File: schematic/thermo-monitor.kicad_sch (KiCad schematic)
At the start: 17 parts, among them J1 AudioJack4, J2 AudioJack4, J3 AudioJack4, J4 AudioJack4, J5 AudioJack4, J6 Barrel_Jack_Switch, SW1 SW_Push_Dual_x2, SW2 SW_Push_Dual_x2, U3 DS18B20, U4 PJ-320A, U8 TFT_320x240

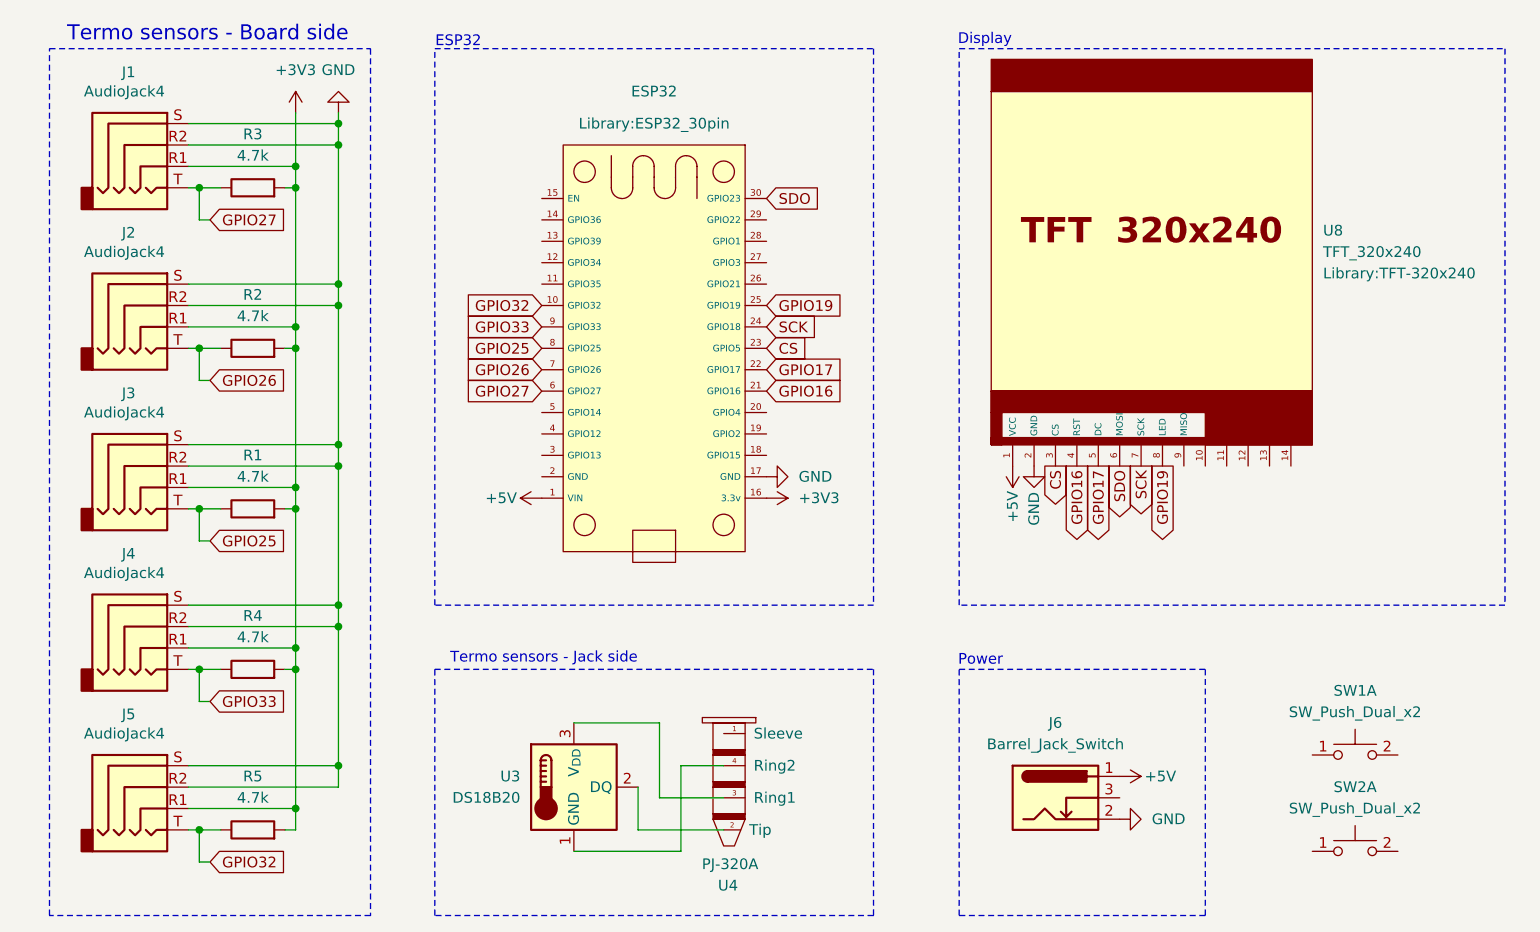
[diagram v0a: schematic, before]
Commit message: feat: buttons on schematic
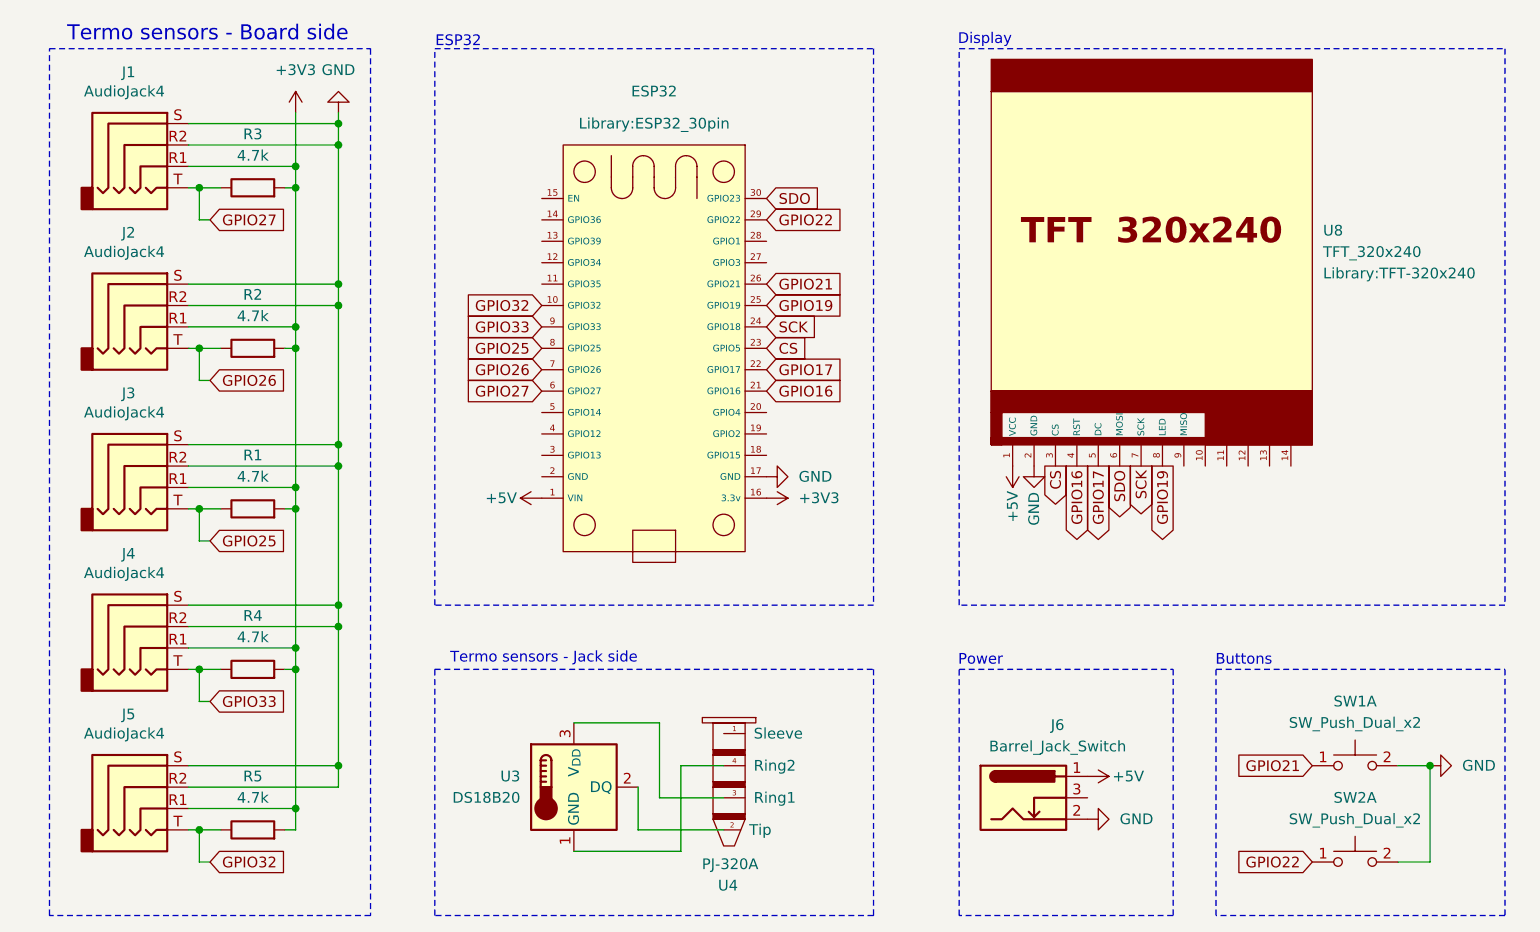
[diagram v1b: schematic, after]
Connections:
- net GND: now also SW1.2 (D), SW2.2 (D)
- net GPIO21: now reaches ESP32.26 (GPIO21)
- net GPIO21: now also SW1.1 (C)
- net GPIO22: now reaches ESP32.29 (GPIO22)
- net GPIO22: now also SW2.1 (C)
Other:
- note added: "Buttons"
- moved on the sheet: J6, SW1A, SW2A

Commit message: fix psu 5v barell rotation
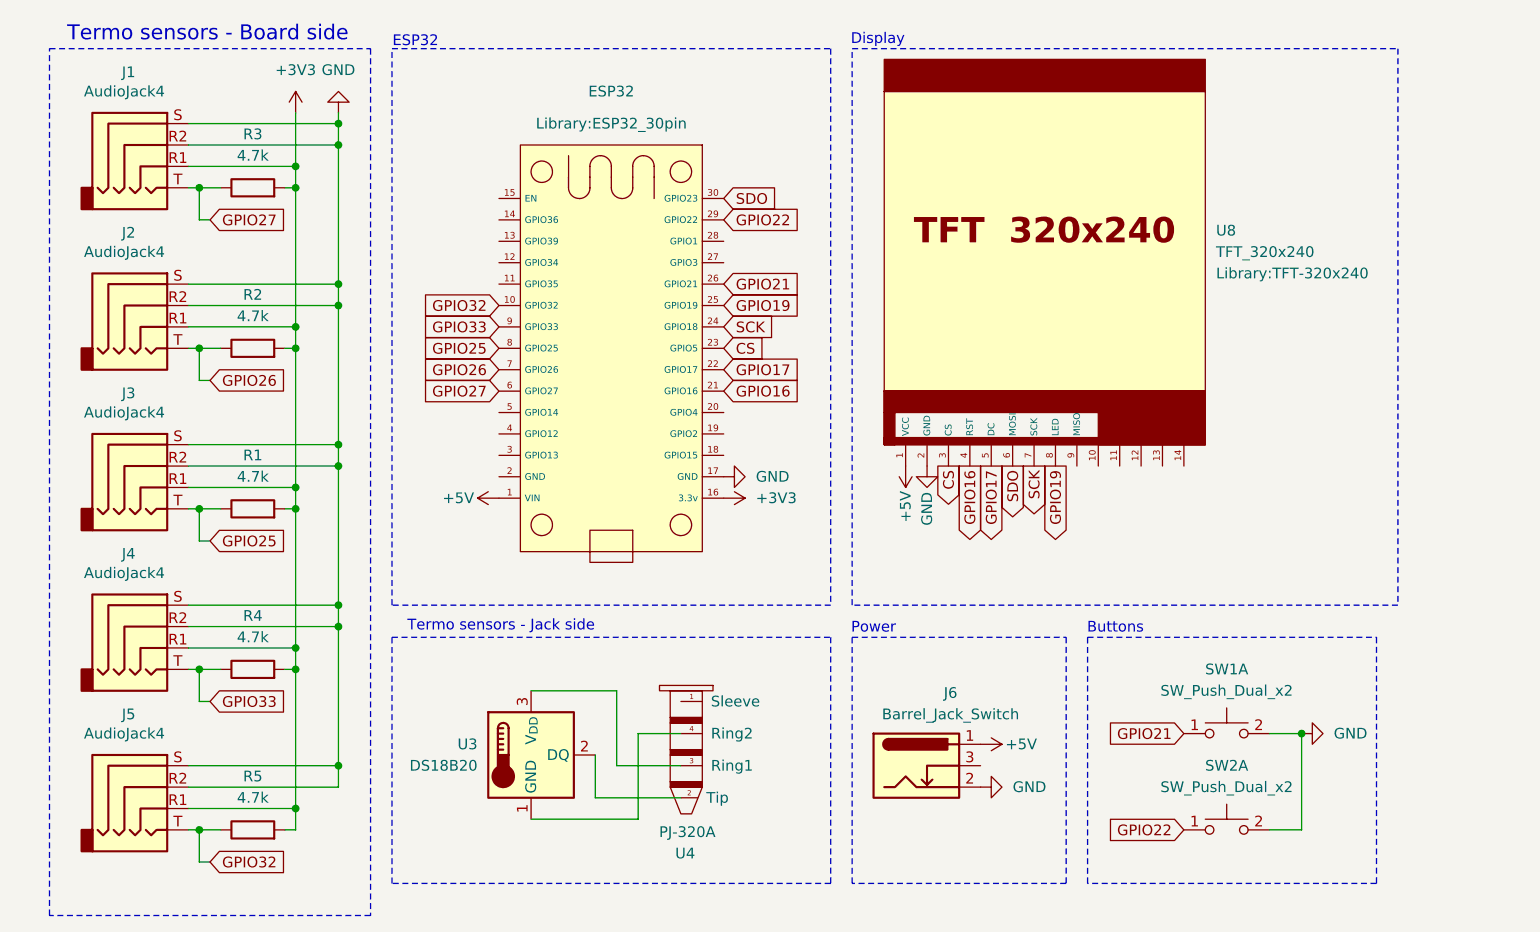
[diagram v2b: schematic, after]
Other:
- moved on the sheet: ESP32, J6, SW1A, SW2A, U3, U4, U8
